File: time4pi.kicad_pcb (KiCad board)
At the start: 4 copper layers, 30.1 x 65.1 mm, 17 parts, among them J1 Raspberry_Pi_2_3, J2 Conn_02x03_Odd_Even, J3 Conn_Coaxial_Small, J4 Conn_Coaxial_Small, Q3 BFR92, Q4 BFR92, U1 ECOC 7050, U2 HMC361S8G/361S8GE, U3 ADF4158, U4 AB0805

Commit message: feat: added logos
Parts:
- added G***: LOGO, LSI:Heimonen-Solutions, F.Cu at (111.0, 55.5)
- added G***: LOGO, LSI:lsi-logo-20mm, F.Cu at (111.0, 52.8)
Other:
- board text added: "time4pi"

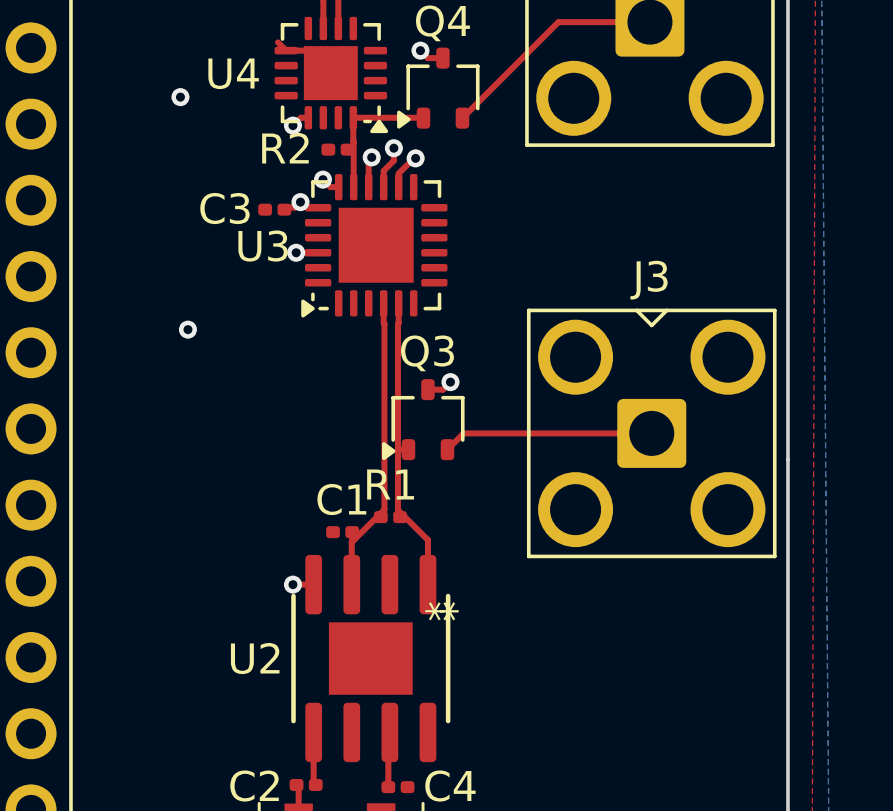
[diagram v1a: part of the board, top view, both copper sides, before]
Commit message: feat: smalled siklscreen text
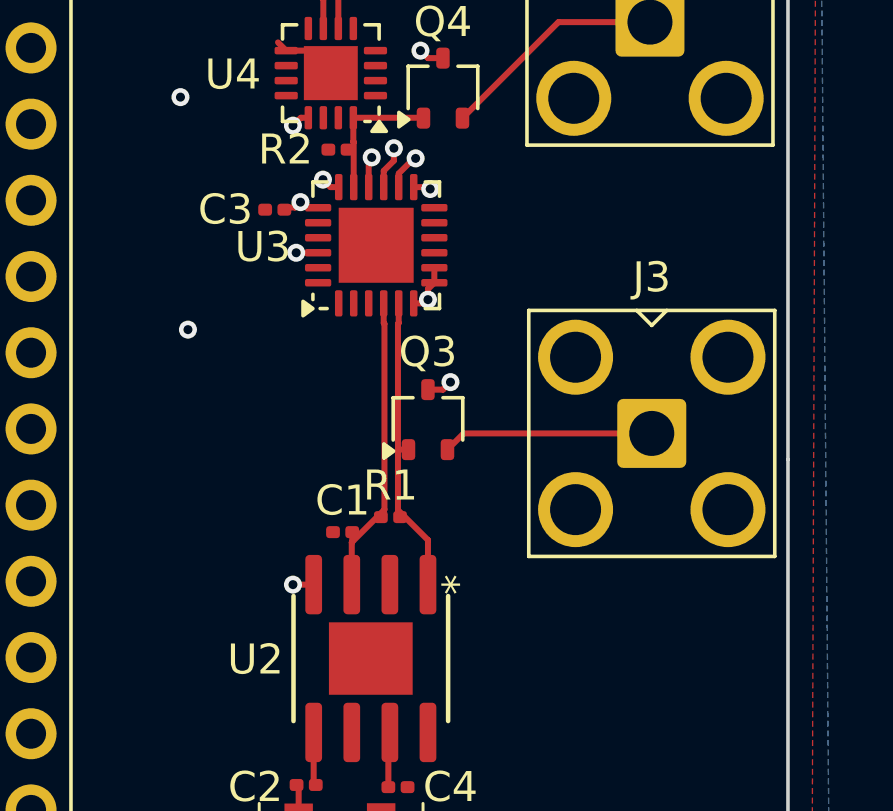
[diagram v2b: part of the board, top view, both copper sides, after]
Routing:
- net +3.3V: track 2.68 -> 4.93 mm, vias 4 -> 6
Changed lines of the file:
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@@
 		)
 		(fp_text user "*"
-			(at -1.5748 2.4614 90)
-			(layer "F.SilkS")
-			(effects
-				(font
-					(size 1 1)
-					(thickness 0.15)
-				)
-			)
-		)
-		(fp_text user "*"
-			(at -1.5748 2.4614 -90)
-			(unlocked yes)
+			(at -2.4638 1.9302 90)
 			(layer "F.SilkS")
 			(effects
@@
 	)
 	(segment
+		(start 110.375 77.625)
+		(end 110.5 77.5)
+		(width 0.2)
+		(layer "F.Cu")
+		(net 4)
+	)
+	(segment
+		(start 110.512894 73.75)
+		(end 110.575395 73.812501)
+		(width 0.2)
+		(layer "F.Cu")
+		(net 4)
+	)
+	(segment
+		(start 110.025 73.75)
+		(end 110.512894 73.75)
+		(width 0.2)
+		(layer "F.Cu")
+		(net 4)
+	)
+	(segment
 		(start 105.775 74.43)
 		(end 106.07 74.43)
@@
 	)
 	(segment
+		(start 110.7125 76.4375)
+		(end 110.7125 76.9375)
+		(width 0.2)
+		(layer "F.Cu")
+		(net 4)
+	)
+	(segment
+		(start 110.5 77.15)
+		(end 110.7125 76.9375)
+		(width 0.2)
+		(layer "F.Cu")
+		(net 4)
+	)
+	(segment
 		(start 107.525 73.75)
 		(end 107.25 73.75)
@@
 	)
 	(segment
+		(start 110.025 77.625)
+		(end 110.375 77.625)
+		(width 0.2)
+		(layer "F.Cu")
+		(net 4)
+	)
+	(segment
 		(start 106.07 74.43)
 		(end 106.25 74.25)
@@
 		(net 4)
 	)
+	(segment
+		(start 110.5 77.5)
+		(end 110.5 77.15)
+		(width 0.2)
+		(layer "F.Cu")
+		(net 4)
+	)
 	(via
 		(at 107 73.5)
@@
 		(size 0.6)
 		(drill 0.3)
+		(layers "F.Cu" "B.Cu")
+		(net 4)
+	)
+	(via
+		(at 110.5 77.5)
+		(size 0.6)
+		(drill 0.3)
+		(layers "F.Cu" "B.Cu")
+		(free yes)
+		(net 4)
+	)
+	(via
+		(at 110.575395 73.812501)
+		(size 0.6)
+		(drill 0.3)

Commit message: feat: more caps
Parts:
- added C10: 10uf, Capacitor_Tantalum_SMD:CP_EIA-3216-10_Kemet-I, F.Cu at (104.5, 89.5)
- added C11: 1000pF, Capacitor_SMD:C_0201_0603Metric, F.Cu at (105.5, 86.5)
- added C5: 10uf, Capacitor_SMD:C_0201_0603Metric, F.Cu at (106.5, 102.0)
- added C6: 0.1uf, Capacitor_SMD:C_0201_0603Metric, F.Cu at (105.0, 102.0)
- added C7: 15pf, Capacitor_SMD:C_0201_0603Metric, F.Cu at (105.0, 93.7)
- added C8: 100pf, Capacitor_SMD:C_0201_0603Metric, F.Cu at (108.5, 85.0)
- added C9: 100pf, Capacitor_SMD:C_0201_0603Metric, F.Cu at (110.0, 85.0)
- C2: value 31.8pF -> 100pF
- moved C1 6.61 mm to (108.6, 78.7)
- moved Q3 0.50 mm to (110.5, 81.0)
- moved R1 0.50 mm to (109.3, 84.3)
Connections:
- U2 pad 1: /5GHz_P -> Net-(U2-OUT_180°)
- U2 pad 3: /5GHz_N -> Net-(U2-OUT)
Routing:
- net /5GHz_N: track 10.9 -> 8.15 mm
- net /5GHz_P: track 10.9 -> 8.55 mm
- net +5V: track 3.13 -> 5.39 mm
- net Net-(U2-OUT): track 0.00 -> 2.09 mm
- net Net-(U2-OUT_180°): track 0.00 -> 2.07 mm
- net +3.3V: track 4.93 -> 6.88 mm
- net Net-(U1-Output): track 1.29 -> 2.10 mm

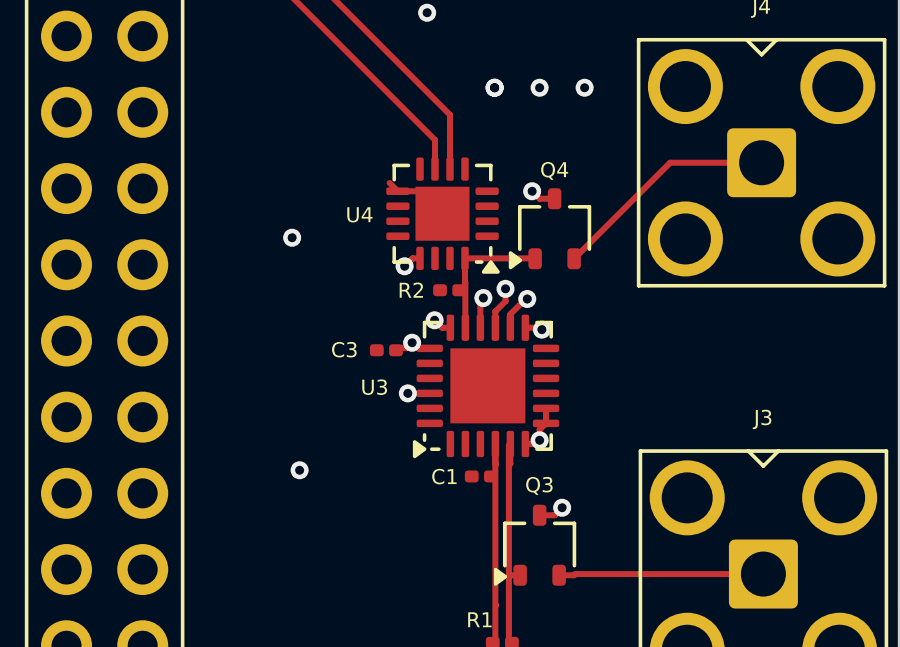
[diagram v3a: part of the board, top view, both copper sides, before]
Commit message: fix: differential pairs
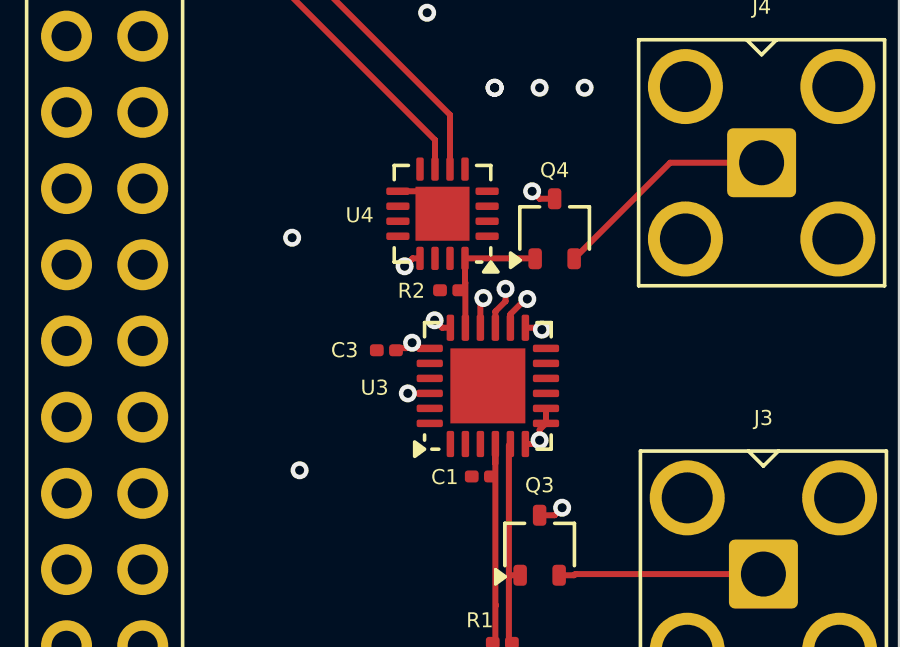
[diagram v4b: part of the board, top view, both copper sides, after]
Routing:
- net /5GHz_P: track 8.55 -> 7.86 mm
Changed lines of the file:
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@@
-		(net 1)
-	)
-	(segment
-		(start 105.775 69.2)
-		(end 105.5 68.925)
-		(width 0.2)
-		(layer "F.Cu")
 		(net 1)
 	)
@@
 	)
 	(segment
-		(start 109.025 78.281251)
-		(end 109.05 78.306251)
-		(width 0.2)
-		(layer "F.Cu")
-		(net 58)
-	)
-	(segment
 		(start 108.82 84.654999)
 		(end 108.82 85)
@@
 	)
 	(segment
-		(start 109.525 77.625)
-		(end 109.525 78.281251)
-		(width 0.2)
-		(layer "F.Cu")
-		(net 59)
-	)
-	(segment
 		(start 109.85 82)
 		(end 109.475 82)
@@
 		(width 0.2)
 		(layer "F.Cu")
-		(net 59)
-	)
-	(segment
-		(start 109.525 78.281251)
-		(end 109.5 78.306251)
-		(width 0.2)
-		(layer "F.Cu")

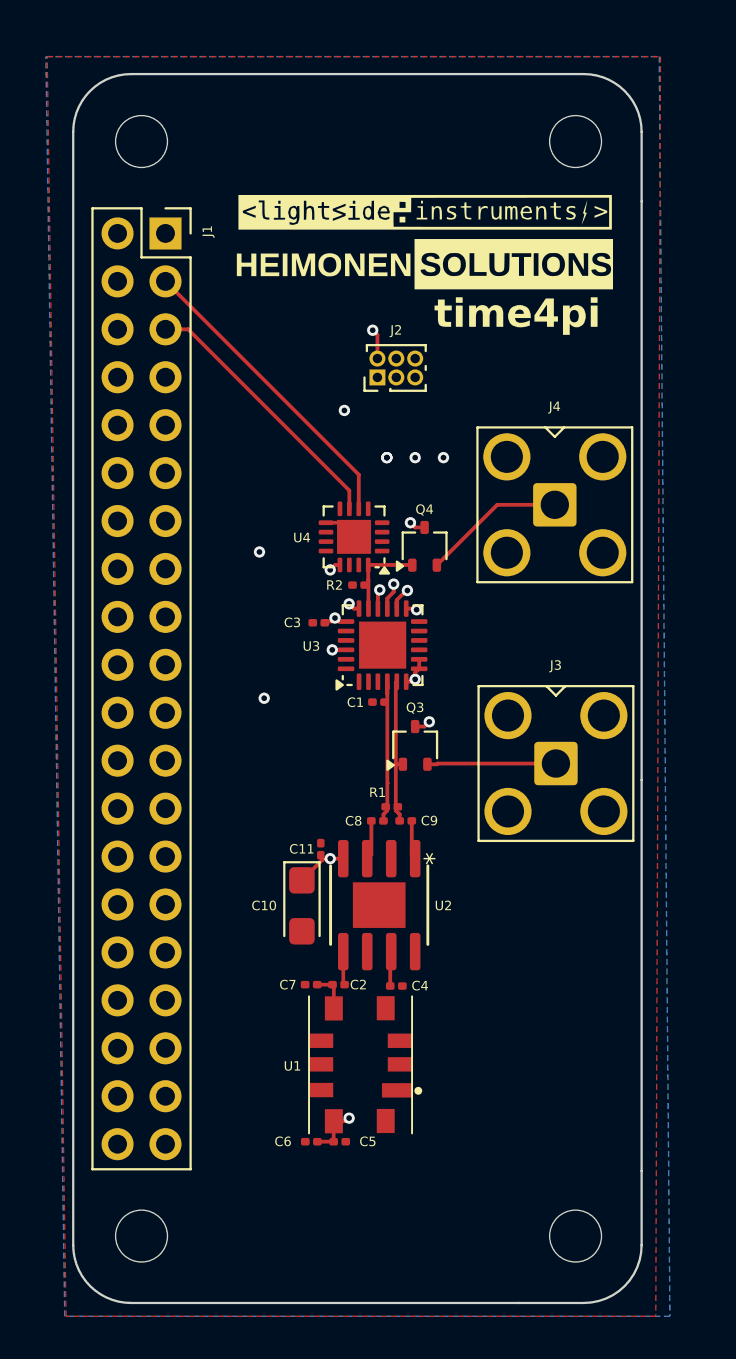
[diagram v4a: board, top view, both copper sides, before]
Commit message: feat: added stitched vias
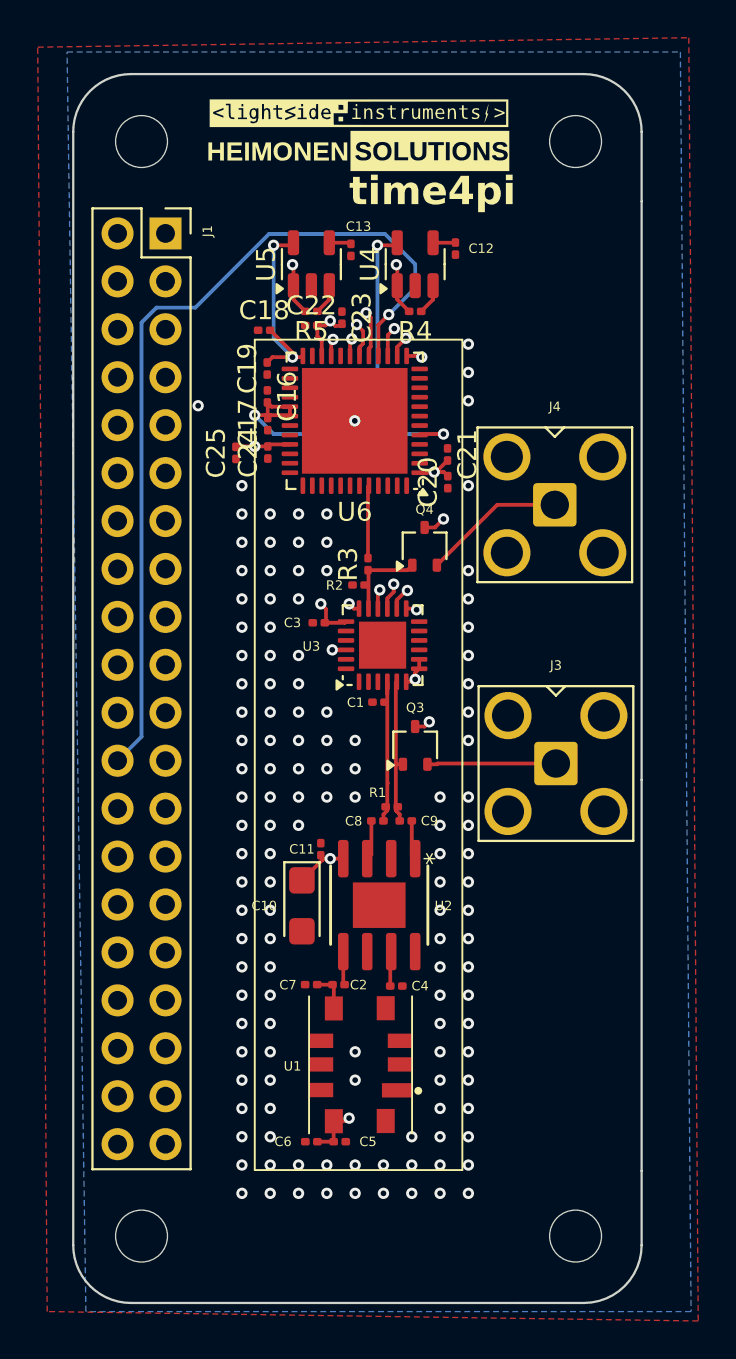
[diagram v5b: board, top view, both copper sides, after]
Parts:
- removed the G*** at (111.0, 55.5)
- removed the G*** at (111.0, 52.8)
- removed J2: Conn_02x03_Odd_Even, Connector_PinHeader_1.00mm:PinHeader_2x03_P1.00mm_Vertical
- added C12: 10nF, Capacitor_SMD:C_0201_0603Metric, F.Cu at (112.6, 54.7)
- added C13: 10nF, Capacitor_SMD:C_0201_0603Metric, F.Cu at (107.1, 54.7)
- added C16: 1uF, Capacitor_SMD:C_0201_0603Metric, F.Cu at (102.7, 62.5)
- added C17: 0.1uF, Capacitor_SMD:C_0201_0603Metric, F.Cu at (102.7, 64.0)
- added C18: 1uF, Capacitor_SMD:C_0201_0603Metric, F.Cu at (102.5, 59.0)
- added C19: 0.1uF, Capacitor_SMD:C_0201_0603Metric, F.Cu at (102.7, 61.0)
- added C20: 0.1uF, Capacitor_SMD:C_0201_0603Metric, F.Cu at (112.2, 67.0)
- added C21: 10uF, Capacitor_SMD:C_0201_0603Metric, F.Cu at (112.2, 65.6)
- added C22: 10uF, Capacitor_SMD:C_0201_0603Metric, F.Cu at (105.0, 58.7)
- added C23: 0.1uF, Capacitor_SMD:C_0201_0603Metric, F.Cu at (106.6, 58.3)
- added C24: 10uF, Capacitor_SMD:C_0201_0603Metric, F.Cu at (102.7, 65.5)
- added C25: 0.1uF, Capacitor_SMD:C_0201_0603Metric, F.Cu at (101.0, 65.5)
- added G***: LOGO, LSI:lsi-logo-16, F.Cu at (107.5, 47.5)
- added G***: LOGO, LSI:heimonen-solutions-16, F.Cu at (107.5, 49.5)
- added R3: 33 Ohm, Resistor_SMD:R_0201_0603Metric, F.Cu at (108.0, 71.4)
- added R4: 100k, Resistor_SMD:R_0201_0603Metric, F.Cu at (110.5, 58.0)
- added R5: 100k, Resistor_SMD:R_0201_0603Metric, F.Cu at (105.0, 58.0)
- added U5: LT1761-2.5, Package_TO_SOT_SMD:TSOT-23-5, F.Cu at (105.0, 55.5)
- added U6: ICE40UP5K-SG48ITR, Package_DFN_QFN:QFN-48-1EP_7x7mm_P0.5mm_EP5.6x5.6mm, F.Cu at (107.3, 63.8)
- U4: value AB0805 -> LT1761-1.2; footprint Package_DFN_QFN:VQFN-16-1EP_3x3mm_P0.5mm_EP1.8x1.8mm -> Package_TO_SOT_SMD:TSOT-23-5
- moved U4 14.8 mm to (110.5, 55.5), turned to 90 degrees
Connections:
- J1 pad 10: /LE_RPI -> unconnected-(J1-GPIO15/RXD-Pad10)
- J1 pad 13: /DATA_RPI -> /CRESET
- J1 pad 19: unconnected-(J1-MOSI0/GPIO10-Pad19) -> /SPI_SI
- J1 pad 21: unconnected-(J1-MISO0/GPIO9-Pad21) -> /SPI_SO
- J1 pad 23: /CLK_RPI -> /SPI_SCK
- J1 pad 24: unconnected-(J1-~{CE0}/GPIO8-Pad24) -> /SPI_SS
- J1 pad 3: SDA -> unconnected-(J1-SDA/GPIO2-Pad3)
- J1 pad 5: SCL -> unconnected-(J1-SCL/GPIO3-Pad5)
- U3 pad 14: /CLK -> /PLL_CLK
- U3 pad 15: /DATA -> /PLL_DATA
- U3 pad 16: /LE -> /PLL_LE
- U4 pad 1: unconnected-(U4-NC-Pad1) -> +3.3V
- U4 pad 2: unconnected-(U4-WDI-Pad2) -> GND
- U4 pad 3: unconnected-(U4-NC-Pad3) -> Net-(U4-~{SHDN})
- U4 pad 4: unconnected-(U4-~{IRQ2}-Pad4) -> Net-(U4-BYP)
- U4 pad 5: unconnected-(U4-VBAT-Pad5) -> +1V2
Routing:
- net /SPI_SS: track 0.00 -> 46.5 mm, vias 0 -> 1
- net /SPI_SCK: track 0.00 -> 38.5 mm, vias 0 -> 2
- net /SPI_SO: track 0.00 -> 36.6 mm, vias 0 -> 1
- net /CLK_RPI: track 34.8 -> 0.00 mm
- net +1V2: track 0.00 -> 27.4 mm, vias 0 -> 3
- net /SPI_SI: track 0.00 -> 27.1 mm, vias 0 -> 1
- net /CRESET: track 0.00 -> 18.6 mm, vias 0 -> 1
- net /LE_RPI: track 18.2 -> 0.00 mm, vias 1 -> 0
- net /PLL_CLK: track 0.00 -> 17.4 mm, vias 0 -> 2
- net /DATA_RPI: track 16.7 -> 0.00 mm
- net SDA: track 16.3 -> 0.00 mm
- net /PLL_LE: track 0.00 -> 16.3 mm, vias 0 -> 2
- net +3.3V: track 6.88 -> 22.2 mm, vias 6 -> 10
- net /PLL_DATA: track 0.00 -> 14.9 mm, vias 0 -> 2
- net SCL: track 14.3 -> 0.00 mm
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
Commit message: feat: bottom and top layer gnd filled
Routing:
- added copper zone on In1.Cu, net +3.3V
- added copper zone on In2.Cu, net +5V
- added copper zone on B.Cu, net GND
- removed copper zone on In2.Cu, net +3.3V
- removed copper zone on B.Cu, net +5V
- removed copper zone on In1.Cu, net GND
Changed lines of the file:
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@@
 			(remove_unused_layers yes)
 			(keep_end_layers yes)
-			(zone_layer_connections "In1.Cu")
+			(zone_layer_connections)
 			(net 1 "GND")
 			(pinfunction "Ext")
@@
 			(remove_unused_layers yes)
 			(keep_end_layers yes)
-			(zone_layer_connections "In1.Cu")
+			(zone_layer_connections)
 			(net 1 "GND")
 			(pinfunction "Ext")
@@
 			(remove_unused_layers yes)
 			(keep_end_layers yes)
-			(zone_layer_connections "In1.Cu")
+			(zone_layer_connections)
 			(net 1 "GND")
 			(pinfunction "Ext")
@@
 			(remove_unused_layers yes)
 			(keep_end_layers yes)
-			(zone_layer_connections "In1.Cu")
+			(zone_layer_connections)
 			(net 1 "GND")
 			(pinfunction "Ext")
@@
 			(remove_unused_layers yes)
 			(keep_end_layers yes)
-			(zone_layer_connections "In1.Cu")
+			(zone_layer_connections)
 			(net 1 "GND")
 			(pinfunction "Ext")
@@
 			(remove_unused_layers yes)
 			(keep_end_layers yes)
-			(zone_layer_connections "In1.Cu")
+			(zone_layer_connections)
 			(net 1 "GND")
 			(pinfunction "Ext")
@@
 			(remove_unused_layers yes)
 			(keep_end_layers yes)
-			(zone_layer_connections "In1.Cu")
+			(zone_layer_connections)
 			(net 1 "GND")
 			(pinfunction "Ext")
@@
 			(remove_unused_layers yes)
 			(keep_end_layers yes)
-			(zone_layer_connections "In1.Cu")
+			(zone_layer_connections)
 			(net 1 "GND")
 			(pinfunction "Ext")
@@
 	)
 	(zone
-		(net 1)
-		(net_name "GND")
+		(net 4)
+		(net_name "+3.3V")
 		(layer "In1.Cu")
 		(hatch edge 0.5)
@@
 	)
 	(zone
-		(net 4)
-		(net_name "+3.3V")
+		(net 8)
+		(net_name "+5V")
 		(layer "In2.Cu")
 		(hatch edge 0.5)
@@
 	)
 	(zone
-		(net 8)
-		(net_name "+5V")
+		(net 1)
+		(net_name "GND")
 		(layer "B.Cu")
 		(hatch edge 0.5)
